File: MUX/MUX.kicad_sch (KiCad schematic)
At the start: 139 parts, among them P1 Conn_02x36_Top_Bottom, P2 DB9_Male, P3 DB9_Male, P4 DB9_Male, P5 DB9_Male

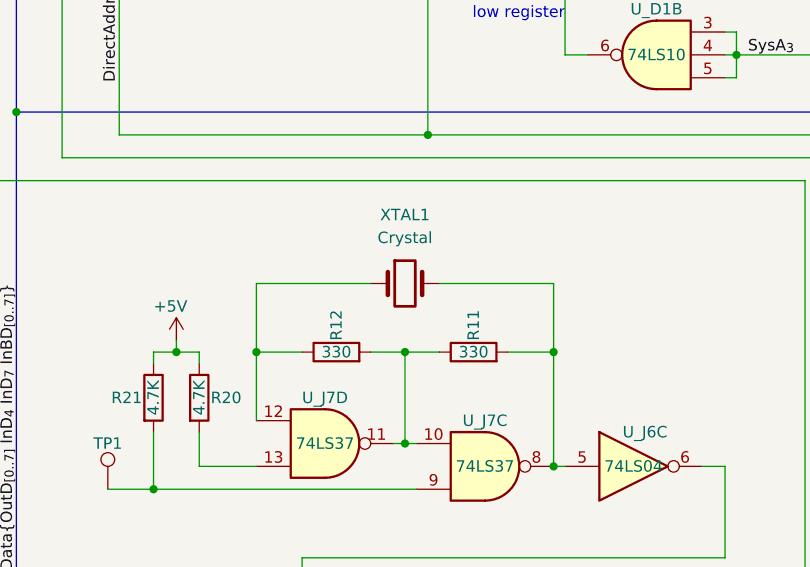
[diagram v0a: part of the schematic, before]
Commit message: MUX: Proper crystal
Use HC-49U crystal. Elements rearranged to match the original layout, just for
fun. Some more power optimizations.
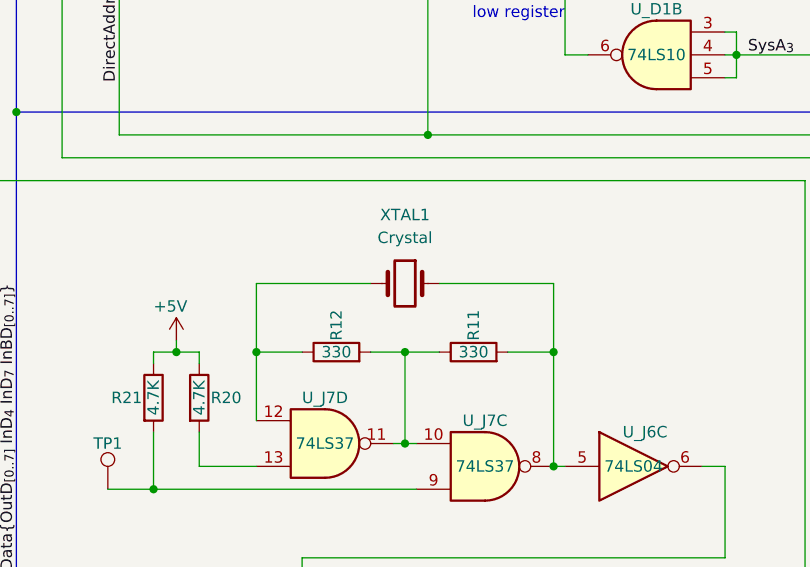
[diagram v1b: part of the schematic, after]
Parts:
- XTAL1: footprint Crystal:Crystal_HC18-U_Vertical -> Crystal:Crystal_HC49-U_Horizontal
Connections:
- net at R11.2, U_J6.5, U_J7.8: now also XTAL1.1; no longer XTAL1.2
- net at R12.1, U_J7.12: now also XTAL1.2; no longer XTAL1.1
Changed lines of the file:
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@@
     (pin "7")
   )
-  (symbol (lib_id "Device:Crystal") (at 172.72 229.87 0) (unit 1)
+  (symbol (lib_id "Device:Crystal") (at 172.72 229.87 0) (mirror y) (unit 1)
     (in_bom yes) (on_board yes) (fields_autoplaced)
     (property "Reference" "XTAL1" (id 0) (at 172.72 222.25 0))
     (property "Value" "Crystal" (id 1) (at 172.72 224.79 0))
-    (property "Footprint" "Crystal:Crystal_HC18-U_Vertical" (id 2) (at 172.72 229.87 0)
+    (property "Footprint" "Crystal:Crystal_HC49-U_Horizontal" (id 2) (at 172.72 229.87 0)
       (effects (font (size 1.27 1.27)) hide)
     )
@@
     )
     (path "/8cf77925-1e00-4e82-8d3f-ed9eca0aa9db"
-      (reference "XTAL1") (unit 1) (value "Crystal") (footprint "Crystal:Crystal_HC18-U_Vertical")
+      (reference "XTAL1") (unit 1) (value "Crystal") (footprint "Crystal:Crystal_HC49-U_Horizontal")
     )
   )

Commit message: MUX: Fix DRC errors
Rearranged U_E4 socket and extra row in order to avoid overlap errors. Fixed up
jumper block courtyards.
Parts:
- U_E4: footprint Package_DIP:DIP-24_W15.24mm -> Package_DIP:DIP-24_W7.62mm
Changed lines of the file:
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@@
     )
     (property "Value" "74LS154" (id 1) (at 266.7 379.73 90))
-    (property "Footprint" "Package_DIP:DIP-24_W15.24mm" (id 2) (at 266.7 379.73 0)
+    (property "Footprint" "Package_DIP:DIP-24_W7.62mm" (id 2) (at 266.7 379.73 0)
       (effects (font (size 1.27 1.27)) hide)
     )
@@
     (in_bom yes) (on_board yes)
     (property "Reference" "U_EB4" (id 0) (at 251.46 320.04 90))
-    (property "Value" "КР1533ИД3" (id 1) (at 262.89 320.04 90))
+    (property "Value" "КР1533ИД3" (id 1) (at 262.89 320.04 90)
+      (effects (font (size 1.27 1.27)) hide)
+    )
     (property "Footprint" "Connector_PinHeader_2.54mm:PinHeader_1x12_P2.54mm_Vertical" (id 2) (at 264.16 323.85 0)
       (effects (font (size 1.27 1.27)) hide)
@@
     )
     (path "/b97dc0b2-4ace-4180-9932-17ae402ec50f"
-      (reference "U_E4") (unit 1) (value "74LS154") (footprint "Package_DIP:DIP-24_W15.24mm")
+      (reference "U_E4") (unit 1) (value "74LS154") (footprint "Package_DIP:DIP-24_W7.62mm")
     )
     (path "/303800f6-36b9-407b-b5bd-652fc580e358"

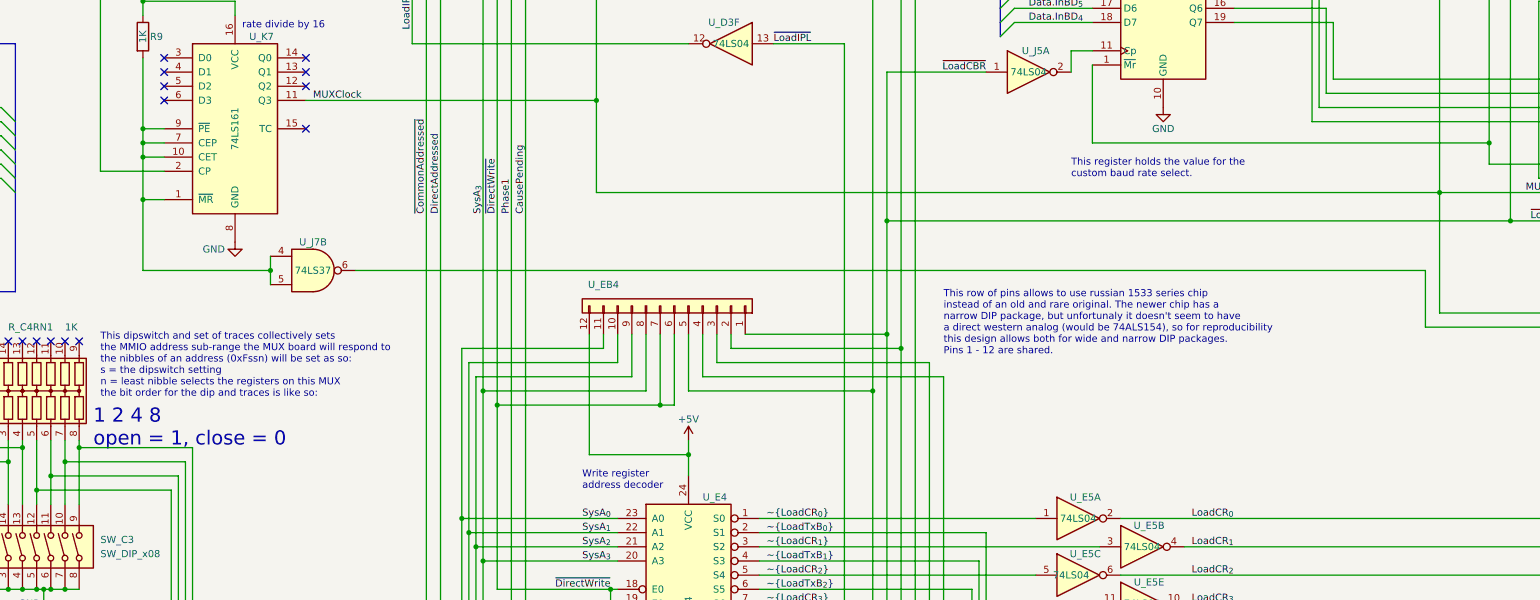
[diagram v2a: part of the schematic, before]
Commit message: MUX: Some polishing
Fix up 3D model a bit, add some notes on the schematic
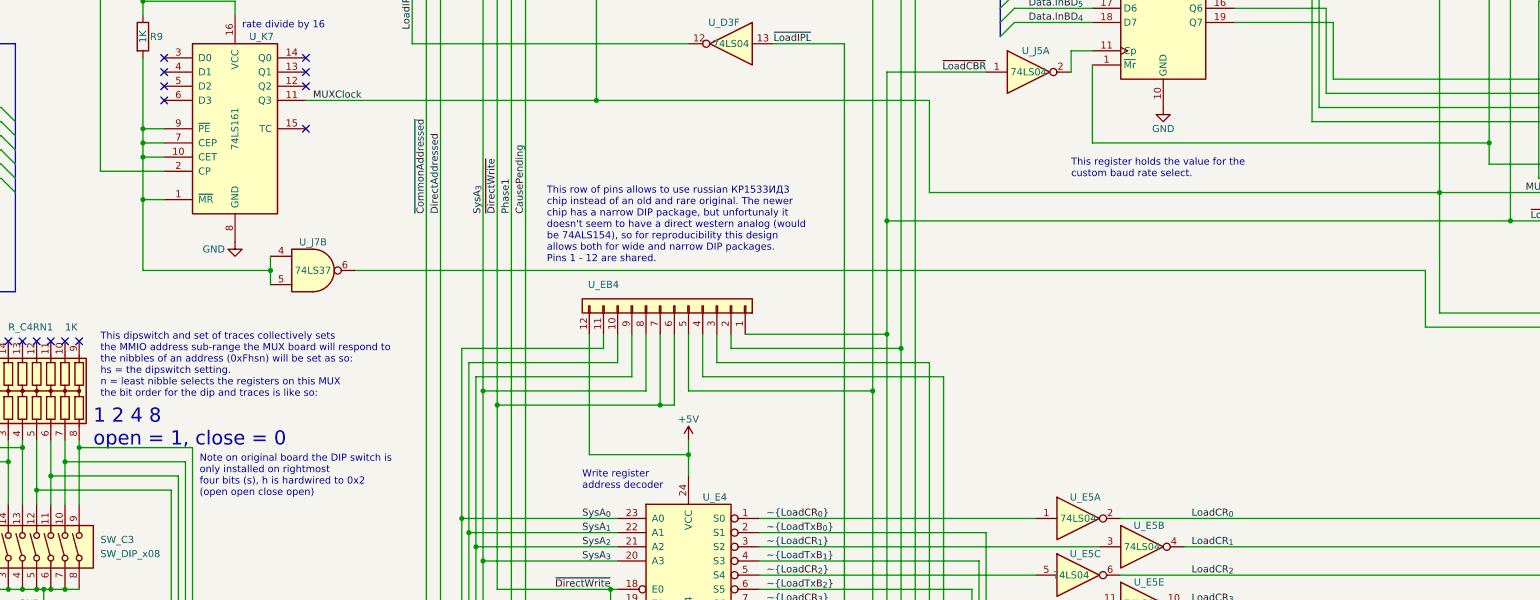
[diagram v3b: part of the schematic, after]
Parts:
- U_EB4: footprint Connector_PinHeader_2.54mm:PinHeader_1x12_P2.54mm_Vertical -> Connector_PinSocket_2.54mm:PinSocket_1x12_P2.54mm_Vertical
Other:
- note added: "Note on original board the DIP switch is only installed on rightmost four bits (s), h is hardwired to 0x2 (open open close open)"
- note added: "This dipswitch and set of traces collectively sets the MMIO address sub-range the MUX board will respond to the nibbles of an address (0xFhsn) will be set as so: hs = the dipswitch setting. n = least nibble selects the registers on this MUX the bit order for the dip and traces is like so:"
- note added: "This row of pins allows to use russian КР1533ИД3 chip instead of an old and rare original. The newer chip has a narrow DIP package, but unfortunaly it doesn't seem to have a direct western analog (would be 74ALS154), so for reproducibility this design allows both for wide and narrow DIP packages. Pins 1 - 12 are shared."
- note removed: "This dipswitch and set of traces collectively sets the MMIO address sub-range the MUX board will respond to the nibbles of an address (0xFssn) will be set as so: s = the dipswitch setting n = least nibble selects the registers on this MUX the bit order for the dip and traces is like so:"
- note removed: "This row of pins allows to use russian 1533 series chip instead of an old and rare original. The newer chip has a narrow DIP package, but unfortunaly it doesn't seem to have a direct western analog (would be 74ALS154), so for reproducibility this design allows both for wide and narrow DIP packages. Pins 1 - 12 are shared."
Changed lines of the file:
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@@
     (stroke (width 0) (type default) (color 0 0 0 0))
   )
-  (wire (pts (xy 250.19 303.53) (xy 401.32 303.53))
+  (wire (pts (xy 309.88 303.53) (xy 401.32 303.53))
     (stroke (width 0) (type default) (color 0 0 0 0))
   )
@@
     (stroke (width 0) (type default) (color 0 0 0 0))
   )
+  (wire (pts (xy 309.88 287.02) (xy 250.19 287.02))
+    (stroke (width 0) (type default) (color 0 0 0 0))
+  )
   (wire (pts (xy 210.82 401.32) (xy 204.47 401.32))
     (stroke (width 0) (type default) (color 0 0 0 0))
@@
     (stroke (width 0) (type default) (color 0 0 0 0))
   )
-  (wire (pts (xy 250.19 287.02) (xy 250.19 303.53))
+  (wire (pts (xy 309.88 287.02) (xy 309.88 303.53))
     (stroke (width 0) (type default) (color 0 0 0 0))
   )
@@
     (effects (font (size 1.27 1.27)) (justify left bottom))
   )
-  (text "This row of pins allows to use russian 1533 series chip\ninstead of an old and rare original. The newer chip has a\nnarrow DIP package, but unfortunaly it doesn't seem to have\na direct western analog (would be 74ALS154), so for reproducibility\nthis design allows both for wide and narrow DIP packages.\nPins 1 - 12 are shared."
-    (at 312.42 332.74 0)
+  (text "This row of pins allows to use russian КР1533ИД3\nchip instead of an old and rare original. The newer\nchip has a narrow DIP package, but unfortunaly it\ndoesn't seem to have a direct western analog (would\nbe 74ALS154), so for reproducibility this design\nallows both for wide and narrow DIP packages.\nPins 1 - 12 are shared."
+    (at 241.3 316.23 0)
     (effects (font (size 1.27 1.27)) (justify left bottom))
   )
@@
     (effects (font (size 1.27 1.27)) (justify left bottom))
   )
-  (text "This dipswitch and set of traces collectively sets\nthe MMIO address sub-range the MUX board will respond to\nthe nibbles of an address (0xFssn) will be set as so:\ns = the dipswitch setting\nn = least nibble selects the registers on this MUX\nthe bit order for the dip and traces is like so:"
+  (text "This dipswitch and set of traces collectively sets\nthe MMIO address sub-range the MUX board will respond to\nthe nibbles of an address (0xFhsn) will be set as so:\nhs = the dipswitch setting.\nn = least nibble selects the registers on this MUX\nthe bit order for the dip and traces is like so:"
     (at 161.29 340.36 0)
     (effects (font (size 1.27 1.27)) (justify left bottom))
@@
     (effects (font (size 1.27 1.27)) (justify left bottom))
   )
+  (text "Note on original board the DIP switch is\nonly installed on rightmost\nfour bits (s), h is hardwired to 0x2\n(open open close open)\n"
+    (at 179.07 358.14 0)
+    (effects (font (size 1.27 1.27)) (justify left bottom))
+  )
   (text "RxDi" (at 896.62 433.07 0)
     (effects (font (size 1.27 1.27)) (justify left bottom))
@@
       (effects (font (size 1.27 1.27)) hide)
     )
-    (property "Footprint" "Connector_PinHeader_2.54mm:PinHeader_1x12_P2.54mm_Vertical" (id 2) (at 264.16 323.85 0)
+    (property "Footprint" "Connector_PinSocket_2.54mm:PinSocket_1x12_P2.54mm_Vertical" (id 2) (at 264.16 323.85 0)
       (effects (font (size 1.27 1.27)) hide)
     )
@@
     )
     (path "/bbc09166-1642-4bfc-87bb-bf13e6998c85"
-      (reference "U_EB4") (unit 1) (value "КР1533ИД3") (footprint "Connector_PinHeader_2.54mm:PinHeader_1x12_P2.54mm_Vertical")
+      (reference "U_EB4") (unit 1) (value "КР1533ИД3") (footprint "Connector_PinSocket_2.54mm:PinSocket_1x12_P2.54mm_Vertical")
     )
     (path "/908892f4-4825-4506-9bd9-8072c2a8c5bc"

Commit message: MUX: Use axial capacitors
Use axial capacitors in order to fully correspond to original board.
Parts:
- C10, C20, C29, C8: footprint Capacitor_THT:CP_Radial_D8.0mm_P3.50mm -> Capacitor_THT:CP_Axial_L25.0mm_D10.0mm_P30.00mm_Horizontal
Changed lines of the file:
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@@
   )
   (text "this gate goes high when:\n0xnn0n is accessed\ndecoding the address common to a bank of MUX boards"
-    (at 81.28 473.71 0)
+    (at 81.28 473.71 180)
     (effects (font (size 1.27 1.27)) (justify right bottom))
   )
@@
   )
   (text "IPL register\nCP is required to load the FF\n~{PE} is a shift (hi) or load (lo) signal\nJ/K are N/C so ~{PE} must always be asserted"
-    (at 81.28 180.34 0)
+    (at 81.28 180.34 180)
     (effects (font (size 1.27 1.27)) (justify right bottom))
   )
@@
   )
   (text "U_B2B matches the high nibble including ~{A_{15}}\nwhich on the CPU6, places the device in\nthe 0x3Fnnn memory range\nfor older buses, it's just 0xFnnn"
-    (at 73.66 374.65 0)
+    (at 73.66 374.65 180)
     (effects (font (size 1.27 1.27)) (justify right bottom))
   )
@@
       (effects (font (size 1.27 1.27)) (justify left))
     )
-    (property "Footprint" "Capacitor_THT:CP_Radial_D8.0mm_P3.50mm" (id 2) (at 801.0652 488.95 0)
+    (property "Footprint" "Capacitor_THT:CP_Axial_L25.0mm_D10.0mm_P30.00mm_Horizontal" (id 2) (at 801.0652 488.95 0)
       (effects (font (size 1.27 1.27)) hide)
     )
@@
       (effects (font (size 1.27 1.27)) (justify left))
     )
-    (property "Footprint" "Capacitor_THT:CP_Radial_D8.0mm_P3.50mm" (id 2) (at 784.5552 488.95 0)
+    (property "Footprint" "Capacitor_THT:CP_Axial_L25.0mm_D10.0mm_P30.00mm_Horizontal" (id 2) (at 784.5552 488.95 0)
       (effects (font (size 1.27 1.27)) hide)
     )
@@
       (effects (font (size 1.27 1.27)) (justify left))
     )
-    (property "Footprint" "Capacitor_THT:CP_Radial_D8.0mm_P3.50mm" (id 2) (at 820.1152 488.95 0)
+    (property "Footprint" "Capacitor_THT:CP_Axial_L25.0mm_D10.0mm_P30.00mm_Horizontal" (id 2) (at 820.1152 488.95 0)
       (effects (font (size 1.27 1.27)) hide)
     )
@@
       (effects (font (size 1.27 1.27)) (justify left))
     )
-    (property "Footprint" "Capacitor_THT:CP_Radial_D8.0mm_P3.50mm" (id 2) (at 820.1152 496.57 0)
+    (property "Footprint" "Capacitor_THT:CP_Axial_L25.0mm_D10.0mm_P30.00mm_Horizontal" (id 2) (at 820.1152 496.57 0)
       (effects (font (size 1.27 1.27)) hide)
     )
@@
     )
     (path "/81dc8f9e-dd81-4ce0-a55c-2233abc8a643"
-      (reference "C8") (unit 1) (value "1000uF") (footprint "Capacitor_THT:CP_Radial_D8.0mm_P3.50mm")
+      (reference "C8") (unit 1) (value "1000uF") (footprint "Capacitor_THT:CP_Axial_L25.0mm_D10.0mm_P30.00mm_Horizontal")
     )
     (path "/700b4e1d-0e7c-4676-a642-620e8cfd527d"
@@
     )
     (path "/cc433d30-73fc-4018-ac68-bb2c058cc5e9"
-      (reference "C10") (unit 1) (value "1000uF") (footprint "Capacitor_THT:CP_Radial_D8.0mm_P3.50mm")
+      (reference "C10") (unit 1) (value "1000uF") (footprint "Capacitor_THT:CP_Axial_L25.0mm_D10.0mm_P30.00mm_Horizontal")
     )
     (path "/91d42fac-90a6-4a10-89bb-f0296fc30e29"
@@
     )
     (path "/3590fe11-f3ef-4623-adbf-cd3168d0b94d"
-      (reference "C20") (unit 1) (value "1000uF") (footprint "Capacitor_THT:CP_Radial_D8.0mm_P3.50mm")
+      (reference "C20") (unit 1) (value "1000uF") (footprint "Capacitor_THT:CP_Axial_L25.0mm_D10.0mm_P30.00mm_Horizontal")
     )
     (path "/0100664a-0ce5-4ad5-a7d8-7afad5973822"
@@
     )
     (path "/17f3a728-3a92-4366-9cf1-82dbfd5924f6"
-      (reference "C29") (unit 1) (value "1000uF") (footprint "Capacitor_THT:CP_Radial_D8.0mm_P3.50mm")
+      (reference "C29") (unit 1) (value "1000uF") (footprint "Capacitor_THT:CP_Axial_L25.0mm_D10.0mm_P30.00mm_Horizontal")
     )
     (path "/abfc0a8c-a849-4ad1-b0b5-5e7c3536fcf4"
